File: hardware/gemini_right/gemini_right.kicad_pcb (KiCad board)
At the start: 2 copper layers, 99.8 x 93.2 mm, 83 parts, among them IC1 XL9555__TSSOP-24_, IC2 ESP32-C3-WROOM-02-N4, J1 Conn_01x02_MountingPin, J1_toLeft1 USB_C_Receptacle_USB2.0_16P, J2 Conn_01x06_MountingPin, J2_toHost1 USB_C_Receptacle_USB2.0_16P, J3_passthrough1 USB_C_Receptacle_USB2.0_16P, SW1 SW_Push, SW10 SW_Push, SW11 SW_Push, SW12 SW_Push, SW13 SW_Push, SW14 SW_Push, SW15 SW_Push, SW16 SW_Push, SW17 SW_Push, SW18 SW_Push, SW19 SW_Push, SW2 SW_Push, SW3 SW_Push, SW4 SW_Push, SW5 SW_Push, SW6 SW_Push, SW7 SW_Push, SW8 SW_Push, SW9 SW_Push, U1 IP5407, U2 XC6206PxxxMR, U3 CH9329, U4 SL2.1s, U5 CW2015CHBD, Y1 Crystal_GND24

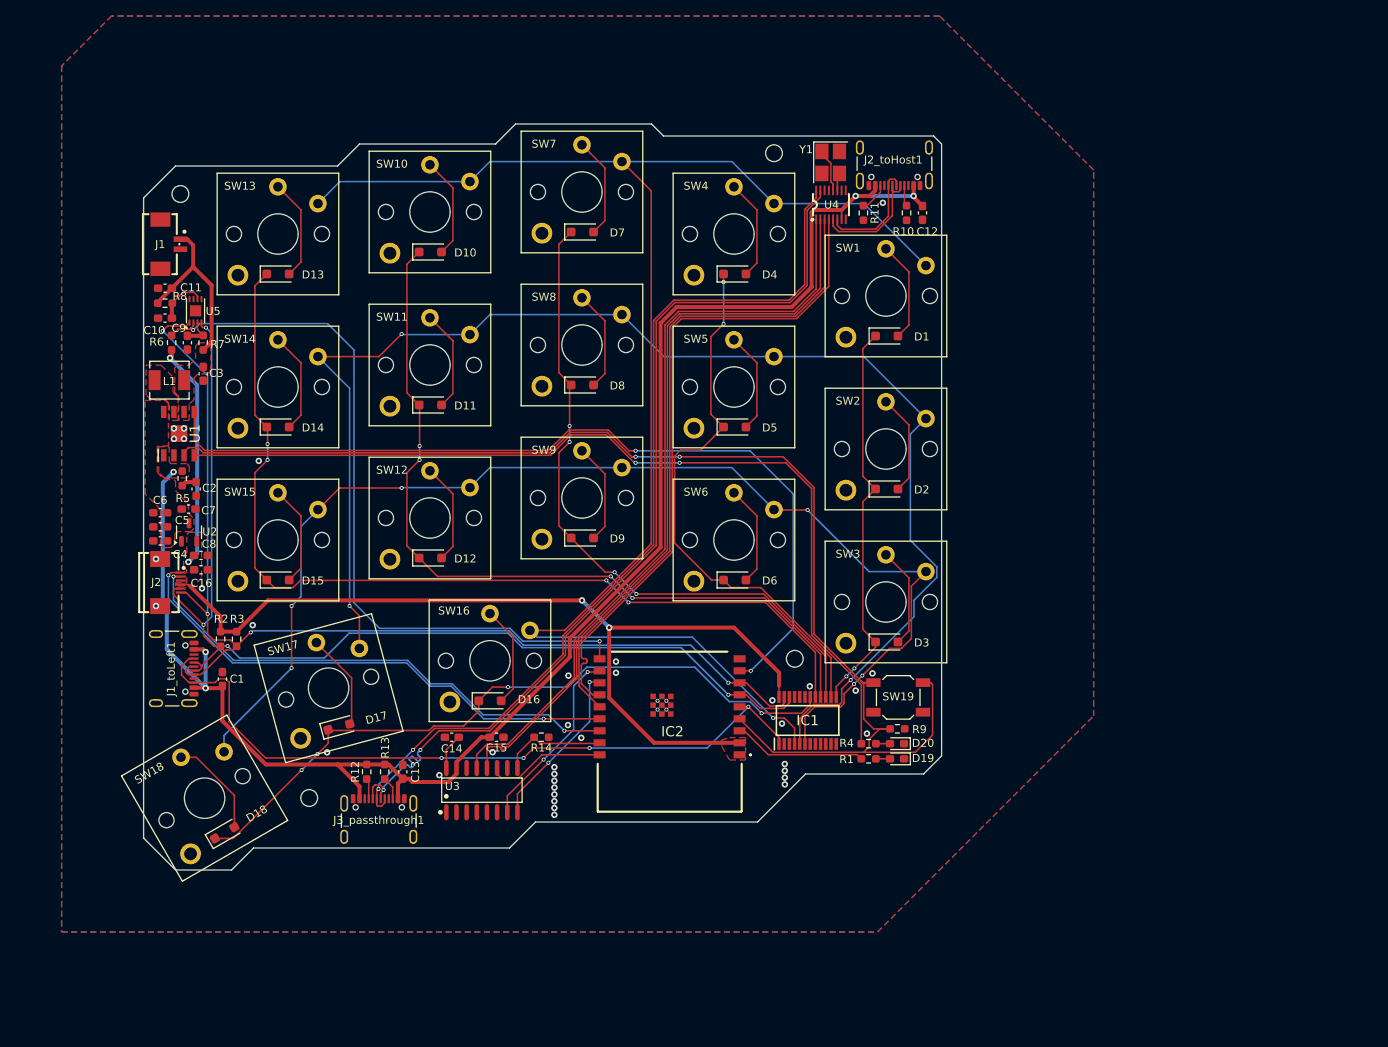
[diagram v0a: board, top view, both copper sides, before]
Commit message: partially finish layout of new design
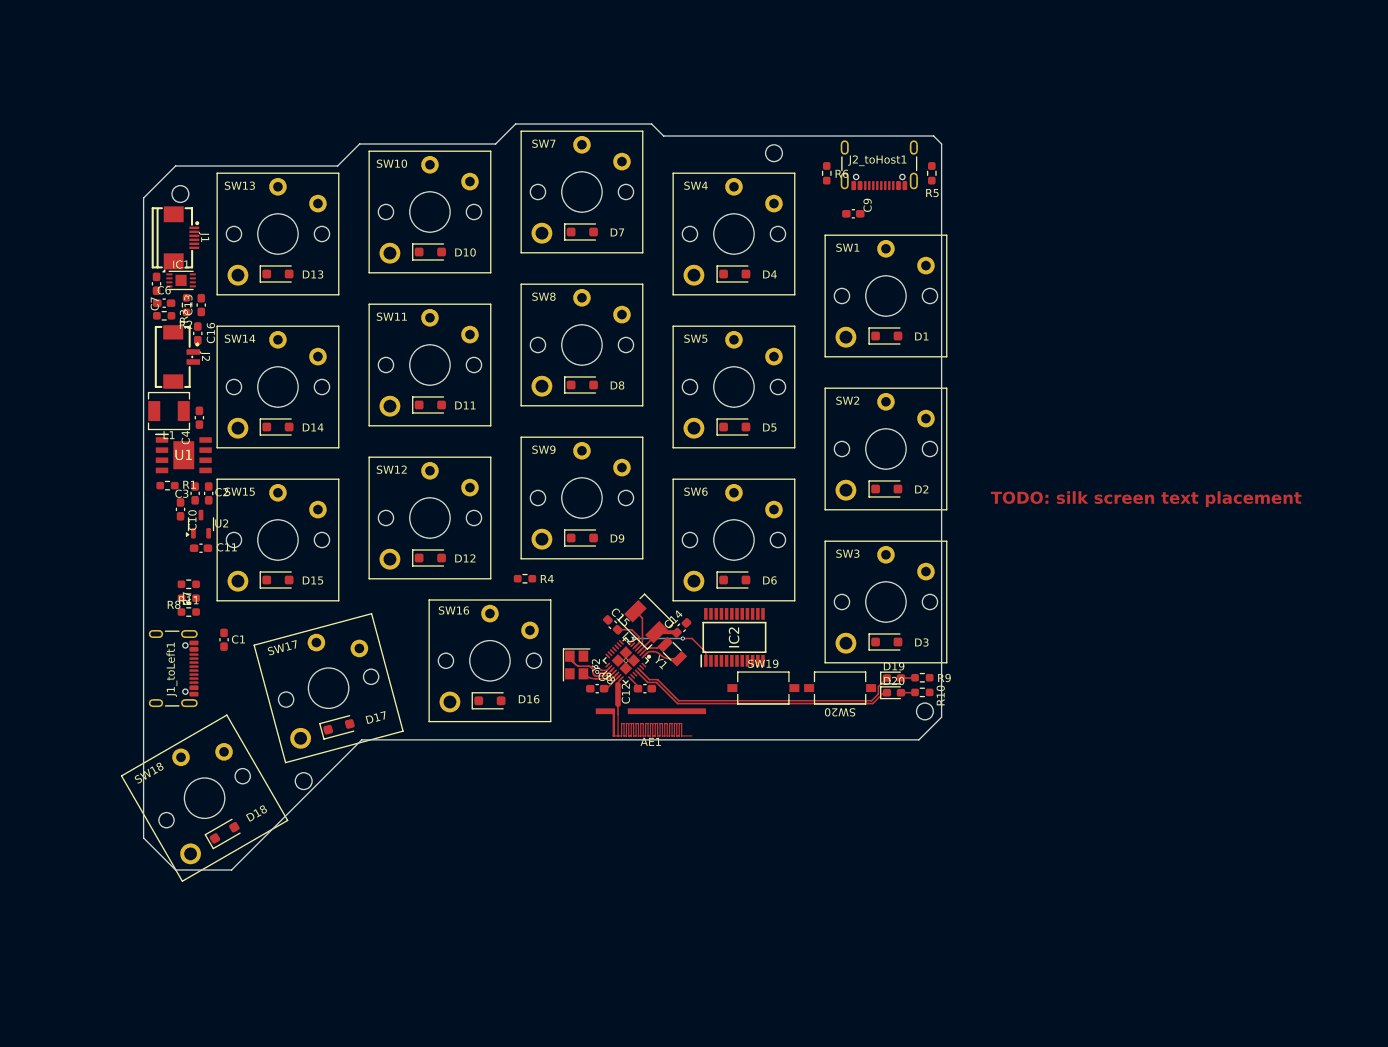
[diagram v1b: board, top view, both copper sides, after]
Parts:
- removed C5: 22uF, Capacitor_SMD:C_0603_1608Metric_Pad1.08x0.95mm_HandSolder
- removed J3_passthrough1: USB_C_Receptacle_USB2.0_16P, Connector_USB:USB_C_Receptacle_GCT_USB4105-xx-A_16P_TopMnt_Horizontal
- removed R12, R13: 56kR, Resistor_SMD:R_0603_1608Metric_Pad0.98x0.95mm_HandSolder
- removed R14: 4.7kR, Resistor_SMD:R_0603_1608Metric_Pad0.98x0.95mm_HandSolder
- removed U4: SL2.1s, ssop-16_L4.6-W2.6-P0.53-LS4.0:SSOP-16_L4.6-W2.6-P0.53-LS4.0-BL
- removed U5: CW2015CHBD, Package_DFN_QFN:TDFN-8-1EP_3x2mm_P0.5mm_EP1.4x1.4mm
- added AE1: Antenna_Shield, chxxx_antenna:ANT-F-3-2.4G-1.6mmFR4-WCH_mirror, F.Cu at (132.6, 111.6)
- added L2: 10uH, Inductor_SMD:L_Chilisin_BMRA00040420, F.Cu at (127.8, 100.0)
- added SW20: SW_Push, Button_Switch_SMD:SW_Tactile_SPST_NO_Straight_CK_PTS636Sx25SMTRLFS, F.Cu at (152.1, 108.3)
- added Y2: 32Mhz 12pF 10ppm, Crystal:Crystal_SMD_3225-4Pin_3.2x2.5mm, F.Cu at (119.1, 105.4)
- C11, C4, C6: value 22uF -> 1uF
- C12: value 10uF -> 0.1uF
- C13: value 10uF -> 2.2uF
- C14: value 100nF -> 0.1uF
- C15: value 100nF -> 1uF
- C16: value 2.2uF -> 22uF
- C2, C3: value 10uF -> 22uF
- C9: value 1uF -> 10uF
- D19: footprint Diode_SMD:D_0603_1608Metric_Pad1.05x0.95mm_HandSolder -> LED_SMD:LED_0603_1608Metric_Pad1.05x0.95mm_HandSolder
- D20: value LED_BLUE -> LED_RED; footprint Diode_SMD:D_0603_1608Metric_Pad1.05x0.95mm_HandSolder -> LED_SMD:LED_0603_1608Metric_Pad1.05x0.95mm_HandSolder
- IC1: value XL9555__TSSOP-24_ -> CW2015CHBD; footprint SOP65P640X120-24N:SOP65P640X120-24N -> Package_DFN_QFN:TDFN-8-1EP_3x2mm_P0.5mm_EP1.4x1.4mm
- IC2: value ESP32-C3-WROOM-02-N4 -> XL9555__TSSOP-24_; footprint ESP32C3WROOM02N4:ESP32C3WROOM02N4 -> SOP65P640X120-24N:SOP65P640X120-24N
- J1: value Conn_01x02_MountingPin -> Conn_01x06_MountingPin; footprint mx1.25_1x02_p1.25:CONN-SMD_2P-P1.25_XUNPU_WAFER-MX1.25-2PWB -> FPC_1x06_p0.5:FPC-SMD_6P-P0.50_XUNPU_FPC-05F-6PH20
- J2: value Conn_01x06_MountingPin -> Conn_01x02_MountingPin; footprint FPC_1x06_p0.5:FPC-SMD_6P-P0.50_XUNPU_FPC-05F-6PH20 -> mx1.25_1x02_p1.25:CONN-SMD_2P-P1.25_XUNPU_WAFER-MX1.25-2PWB
- L1: value 1uH -> 2.2uH; footprint Inductor_SMD:L_Sunlord_MWSA0402S -> Inductor_SMD:L_Chilisin_BMRA00040420
- R1: value 470R -> 56k
- R10: value 5.1kR -> 470r
- R11: value 5.1kR -> 2kR
- R2: value 2kR -> 470r
- R3: value 2kR -> 100r
- R4: value 470R -> 4.7k
- R5: value 2R -> 5.1kR
- R6: value 4.7kR -> 5.1kR
- R7: value 100R -> 2kR
- R8: value 470R -> 2kR
- R9: value 51kR -> 470r
- SW19: footprint Button_Switch_SMD:SW_SPST_SKQG_WithoutStem -> Button_Switch_SMD:SW_Tactile_SPST_NO_Straight_CK_PTS636Sx25SMTRLFS
- U1: value IP5407 -> ETA9742; footprint IP5306_4.35V:SOIC127P600X165-9N -> SOIC127P600X175-9N:SOIC127P600X175-9N
- U3: value CH9329 -> CH582F; footprint sop-16_L9.9-W3.9-P1.27-LS6.0:SOP-16_L9.9-W3.9-P1.27-LS6.0-BL -> chxxx:QFN28_4X4
- Y1: value Crystal_GND24 -> 32.768khz 12.5pF 20ppm; footprint Oscillator:Oscillator_SMD_Abracon_ASE-4Pin_3.2x2.5mm_HandSoldering -> Crystal:Crystal_SMD_3215-2Pin_3.2x1.5mm
- moved R5 101.2 mm to (163.5, 43.9)
- moved R11 98.0 mm to (70.6, 98.8), turned to 0 degrees
- moved IC1 95.7 mm to (69.7, 57.3), turned to 0 degrees
- moved R1 94.1 mm to (68.0, 83.0), turned to 180 degrees
- moved C9 84.8 mm to (153.7, 49.0), turned to 180 degrees
- moved R6 84.6 mm to (150.4, 43.9), turned to -90 degrees
- moved C12 68.9 mm to (127.7, 108.3), turned to 180 degrees
- moved Y1 64.3 mm to (131.1, 103.7), turned to 135 degrees
- moved C13 63.5 mm to (72.2, 60.4), turned to -90 degrees
- moved R10 60.0 mm to (162.3, 108.8), turned to 0 degrees
- moved C8 52.2 mm to (121.7, 108.3)
- moved R4 47.6 mm to (112.7, 94.6), turned to 0 degrees
- moved R2 41.9 mm to (70.4, 60.4), turned to -90 degrees
- moved R3 41.4 mm to (67.6, 61.7), turned to 0 degrees
- moved R8 37.0 mm to (70.6, 97.0), turned to 0 degrees
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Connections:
- C1 pad 1: /VBUS -> +3V3
- C10 pad 1: Net-(U5-CELL) -> GND
- C10 pad 2: GND -> /VBUS
- C11 pad 1: +BATT -> +3V3
- C12 pad 1: /VBUS -> GND
- C12 pad 2: GND -> /VDCIA
- C13 pad 1: /VBUS -> +3V3
- C14 pad 1: Net-(U3-V33) -> /VDCIA
- C15 pad 1: /VBUS -> +3V3
- C16 pad 1: +3V3 -> +BATT
- C2 pad 1: GND -> /VBUS
- C2 pad 2: Net-(C2-Pad2) -> GND
- C3 pad 1: +BATT -> /VBUS
- C4 pad 1: /5VOUT -> GND
- C4 pad 2: GND -> +BATT
- C6 pad 1: /5VOUT -> Net-(IC1-CELL)
- C7 pad 1: GND -> Net-(IC1-VDD)
- C7 pad 2: /5VOUT -> GND
- C8 pad 1: +3V3 -> GND
- C8 pad 2: GND -> Net-(U3-VINTA)
- C9 pad 1: Net-(U5-VDD) -> /VBUS
- D19 pad 1: GND -> /STAT_LED
- D20 pad 1: GND -> /WARN_LED
- IC1 pad 1: /KEY_INT -> GND
- IC1 pad 2: GND -> Net-(IC1-CELL)
- IC1 pad 3: GND -> Net-(IC1-VDD)
- IC1 pad 4: /RCOL0 -> GND
- IC1 pad 5: /RCOL1 -> /PWR_ALRT
- IC1 pad 6: /RCOL2 -> GND
- IC1 pad 7: unconnected-(IC1-P03-Pad7) -> /SCL
- IC1 pad 8: unconnected-(IC1-P04-Pad8) -> /SDA
- IC1 pad 9: unconnected-(IC1-P05-Pad9) -> GND
- IC2 pad 1: +3V3 -> /KEY_INT
- IC2 pad 10: /BAT_INT -> unconnected-(IC2-P06-Pad10)
- IC2 pad 11: /UART0_RX -> unconnected-(IC2-P07-Pad11)
- IC2 pad 12: /UART0_TX -> GND
- IC2 pad 13: /USB_ESP_DP -> /RROW0
- IC2 pad 14: /USB_ESP_DN -> /RROW1
- IC2 pad 15: /TPAD_RDY -> /RROW2
- IC2 pad 16: /TPAD_NRST -> /RROW3
- IC2 pad 17: /USB_HID_TRANSMIT -> /RROW4
- IC2 pad 18: /USB_HID_SET -> /RROW5
- IC2 pad 19: GND -> unconnected-(IC2-P16-Pad19)
- IC2 pad 2: +3V3 -> GND
- IC2 pad 20: GND -> unconnected-(IC2-P17-Pad20)
- IC2 pad 22: GND -> /SCL
- IC2 pad 23: GND -> /SDA
- IC2 pad 24: GND -> +3V3
- IC2 pad 3: /STAT_LED -> GND
- IC2 pad 4: /PWR_BTN -> /RCOL0
- IC2 pad 5: /KEY_INT -> /RCOL1
- IC2 pad 6: /SCL -> /RCOL2
- IC2 pad 7: /SDA -> unconnected-(IC2-P03-Pad7)
- IC2 pad 8: /PWR_STAT -> unconnected-(IC2-P04-Pad8)
- IC2 pad 9: GND -> unconnected-(IC2-P05-Pad9)
- J1 pad 1: +BATT -> /TPAD_RDY
- J1 pad 2: GND -> /TPAD_NRST
- J1_toLeft1 pad A4: /VBUS -> +3V3
- J1_toLeft1 pad A9: /VBUS -> +3V3
- J1_toLeft1 pad B4: /VBUS -> +3V3
- J1_toLeft1 pad B9: /VBUS -> +3V3
- J2 pad 1: /TPAD_RDY -> +BATT
- J2 pad 2: /TPAD_NRST -> GND
- J2_toHost1 pad A6: /USB_DP -> /USB_D+
- J2_toHost1 pad A7: /USB_DN -> /USB_D-
- J2_toHost1 pad B6: /USB_DP -> /USB_D+
- J2_toHost1 pad B7: /USB_DN -> /USB_D-
- L1 pad 1: Net-(U1-SW) -> +BATT
- L1 pad 2: +BATT -> Net-(U1-SW)
- R1 pad 1: /STAT_LED -> Net-(U1-ISET)
- R1 pad 2: Net-(D19-A) -> GND
- R10 pad 1: Net-(J2_toHost1-CC1) -> Net-(D20-A)
- R10 pad 2: GND -> /VBUS
- R11 pad 1: Net-(J2_toHost1-CC2) -> /KEY_INT
- R11 pad 2: GND -> +3V3
- R2 pad 1: /SCL -> Net-(IC1-CELL)
- R2 pad 2: +3V3 -> +BATT
- R3 pad 1: /SDA -> Net-(IC1-VDD)
- R3 pad 2: +3V3 -> +BATT
- R4 pad 1: Net-(D20-A) -> +3V3
- R4 pad 2: Net-(U1-LED1) -> /PWR_ALRT
- R5 pad 1: /VBUS -> Net-(J2_toHost1-CC1)
- R5 pad 2: Net-(C2-Pad2) -> GND
- R6 pad 1: +3V3 -> Net-(J2_toHost1-CC2)
- R6 pad 2: /BAT_INT -> GND
- R7 pad 1: +BATT -> /SCL
- R7 pad 2: Net-(U5-VDD) -> +3V3
- R8 pad 1: Net-(U5-CELL) -> /SDA
- R8 pad 2: +BATT -> +3V3
- R9 pad 1: /PWR_BTN -> Net-(D19-A)
- R9 pad 2: GND -> /VBUS
- SW19 pad 1: /PWR_BTN -> /ISPn
- U1 pad 1: /VBUS -> Net-(U1-SW)
- U1 pad 3: /PWR_BTN -> /PWR_STAT
- U1 pad 4: Net-(U1-LED1) -> /BOOST_STAT
- U1 pad 5: /PWR_STAT -> Net-(U1-ISET)
- U1 pad 7: Net-(U1-SW) -> /VBUS
- U1 pad 8: /5VOUT -> GND
- U2 pad 3: /5VOUT -> /VBUS
- U3 pad 1: unconnected-(U3-ACT#-Pad1) -> /X32k_PIN0
- U3 pad 10: unconnected-(U3-DEF-Pad10) -> /SCL
- U3 pad 11: /USB_HID_SET -> /SDA
- U3 pad 12: /USB_HID_DP -> /USB_D+
- U3 pad 13: /USB_HID_DN -> /USB_D-
- U3 pad 14: GND -> /PWR_ALRT
- U3 pad 15: /VBUS -> unconnected-(U3-PB4/RXD0/PWM7-Pad15)
- U3 pad 16: Net-(U3-V33) -> /RSTn
- U3 pad 2: unconnected-(U3-MODE0-Pad2) -> /X32k_PIN1
- U3 pad 3: unconnected-(U3-MODE1-Pad3) -> /VDCIA
- U3 pad 4: unconnected-(U3-CFG0-Pad4) -> /VSW
- U3 pad 5: unconnected-(U3-CFG1-Pad5) -> +3V3
- U3 pad 7: /UART0_RX -> /KEY_INT
- U3 pad 8: /UART0_TX -> /TPAD_NRST
- U3 pad 9: /USB_HID_TRANSMIT -> /TPAD_RDY
- Y1 pad 1: /XIN -> /X32k_PIN1
- Y1 pad 2: GND -> /X32k_PIN0
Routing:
- net /VBUS: track 202.2 -> 0.00 mm, vias 5 -> 0
- net /RCOL0: track 192.6 -> 0.00 mm, vias 1 -> 0
- net /RCOL1: track 174.1 -> 0.00 mm, vias 3 -> 0
- net /PWR_BTN: track 160.6 -> 0.00 mm, vias 2 -> 0
- net /RCOL2: track 149.2 -> 0.00 mm, vias 6 -> 0
- net +3V3: track 143.3 -> 4.52 mm, vias 4 -> 0
- net /SDA: track 136.2 -> 0.00 mm, vias 4 -> 0
- net /SCL: track 133.6 -> 0.00 mm, vias 4 -> 0
- net /RROW4: track 119.3 -> 0.00 mm, vias 4 -> 0
- net /USB_PASSTHROUGH_DN: track 117.2 -> 0.00 mm, vias 2 -> 0
- net Net-(U1-LED1): track 115.5 -> 0.00 mm, vias 2 -> 0
- net /USB_PASSTHROUGH_DP: track 113.7 -> 0.00 mm, vias 2 -> 0
- net /PWR_STAT: track 109.0 -> 0.00 mm, vias 2 -> 0
- net /RROW3: track 101.3 -> 0.00 mm, vias 4 -> 0
- net /USB_HID_DN: track 96.1 -> 0.00 mm
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- removed copper zone on F.Cu, net +3V3
- removed copper zone on F.Cu, net +BATT
- removed copper zone on F.Cu, net /5VOUT
- removed copper zone on F.Cu, net /VBUS
- removed copper zone on B.Cu, net GND
- removed copper zone on F.Cu, net GND
- removed copper zone on F.Cu, net Net-(U1-SW)
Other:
- outline, holes or cut-outs redrawn
- board text added: "TODO: silk screen text placement"

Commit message: finish routing for right half
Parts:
- moved C4 13.8 mm to (68.2, 87.8), turned to 0 degrees
- moved R4 11.1 mm to (123.3, 97.8), turned to 135 degrees
- moved C10 6.44 mm to (67.7, 92.1), turned to 90 degrees
- moved C11 6.01 mm to (71.6, 96.8), turned to -90 degrees
- moved C2 5.71 mm to (71.6, 89.4), turned to 0 degrees
- moved U2 5.00 mm to (70.5, 92.5)
- moved C13 4.85 mm to (72.0, 55.5)
- moved C7 4.77 mm to (70.2, 60.9)
- moved R3 4.41 mm to (71.9, 62.7), turned to -90 degrees
- moved R2 4.29 mm to (69.2, 64.5), turned to 0 degrees
- moved U1 3.93 mm to (69.9, 83.1), turned to -90 degrees
- moved C3 3.87 mm to (71.6, 87.8), turned to 0 degrees
- moved C6 3.64 mm to (66.5, 63.6), turned to 90 degrees
- moved L1 3.33 mm to (69.8, 76.5), turned to 0 degrees
- moved IC1 2.76 mm to (67.7, 59.2), turned to 90 degrees
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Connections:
- U3 pad 14: /PWR_ALRT -> /TPAD_NRST
- U3 pad 8: /TPAD_NRST -> /PWR_ALRT
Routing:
- net /RCOL0: track 0.00 -> 190.6 mm, vias 0 -> 5
- net /VBUS: track 0.00 -> 187.1 mm, vias 0 -> 5
- net /RCOL1: track 0.00 -> 173.5 mm, vias 0 -> 3
- net /SDA: track 0.00 -> 158.7 mm, vias 0 -> 8
- net /RCOL2: track 0.00 -> 157.0 mm
- net /SCL: track 0.00 -> 156.1 mm, vias 0 -> 8
- net +3V3: track 4.52 -> 140.2 mm, vias 0 -> 3
- net /RROW4: track 0.00 -> 104.3 mm, vias 0 -> 8
- net /TPAD_NRST: track 0.00 -> 94.6 mm
- net /PWR_ALRT: track 0.00 -> 93.7 mm, vias 0 -> 2
- net /TPAD_RDY: track 0.00 -> 93.5 mm
- net /RROW5: track 0.00 -> 91.6 mm, vias 0 -> 2
- net /RROW3: track 0.00 -> 86.2 mm, vias 0 -> 7
- net /BOOST_STAT: track 0.00 -> 81.4 mm, vias 0 -> 4
- net /PWR_STAT: track 0.00 -> 79.1 mm, vias 0 -> 4
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- added copper zone on F.Cu, net +3V3
- added copper zone on F.Cu, net +BATT
- added copper zone on F.Cu, net /BOOST_STAT
- added copper zone on F.Cu, net /ISPn
- added copper zone on F.Cu, net /PWR_STAT
- added copper zone on F.Cu, net /RROW0
- added copper zone on F.Cu, net /RROW1
- added copper zone on F.Cu, net /RROW3
- added copper zone on F.Cu, net /RROW4
- added copper zone on F.Cu, net /RSTn
- added copper zone on F.Cu, net /SCL
- added copper zone on F.Cu, net /SDA
- added copper zone on F.Cu, net /VBUS
- added copper zone on F.Cu, net /VDCIA
- added copper zone on B.Cu, net GND
- added copper zone on F.Cu, net GND
- added copper zone on F.Cu, net Net-(U1-ISET)
- added copper zone on F.Cu, net Net-(U1-SW)
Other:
- outline, holes or cut-outs redrawn
- board text removed: "TODO: silk screen text placement"
